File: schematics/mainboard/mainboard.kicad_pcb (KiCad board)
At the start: 4 copper layers, 88.5 x 180 mm, 94 parts, among them J1 SD_Card_Receptacle, J2 LCD_CONN, J3 USB_C_Receptacle_USB2.0_16P, J4 BATTERY_CONN, J6 HID_CONN, J7 SPEAKER, J8 TRACKBALL_CONN, J9 AudioJack3, P1 1-1473005-4, SW1 SW_SPST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

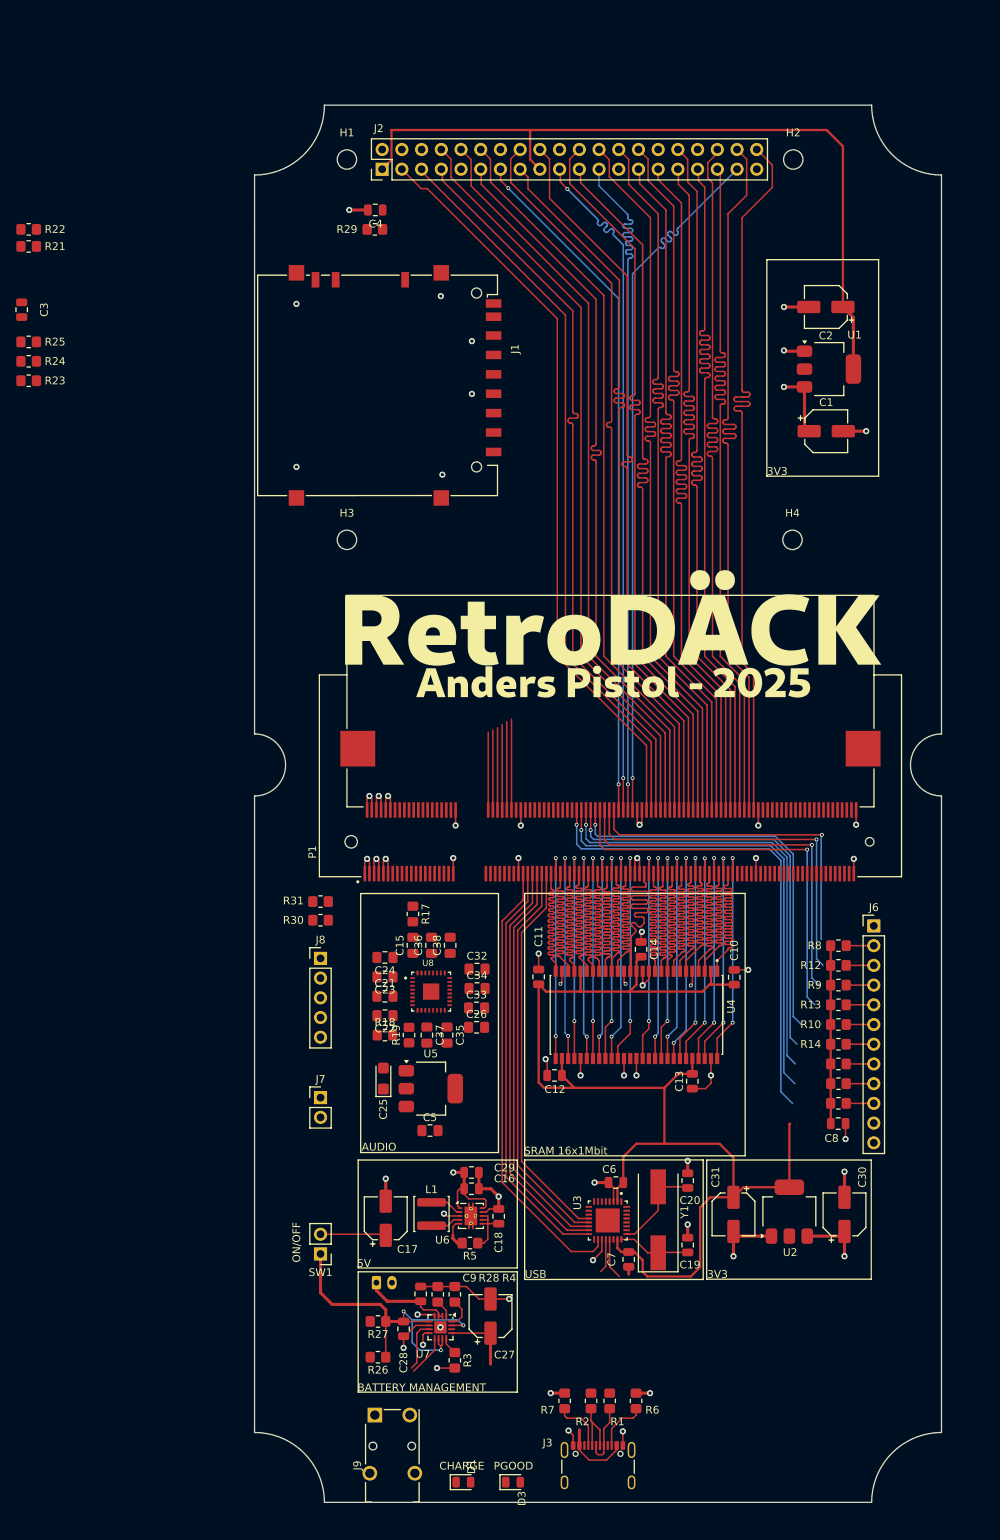
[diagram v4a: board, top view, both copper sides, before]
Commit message: Added "button board". Also placed LCD on main board at correct location.
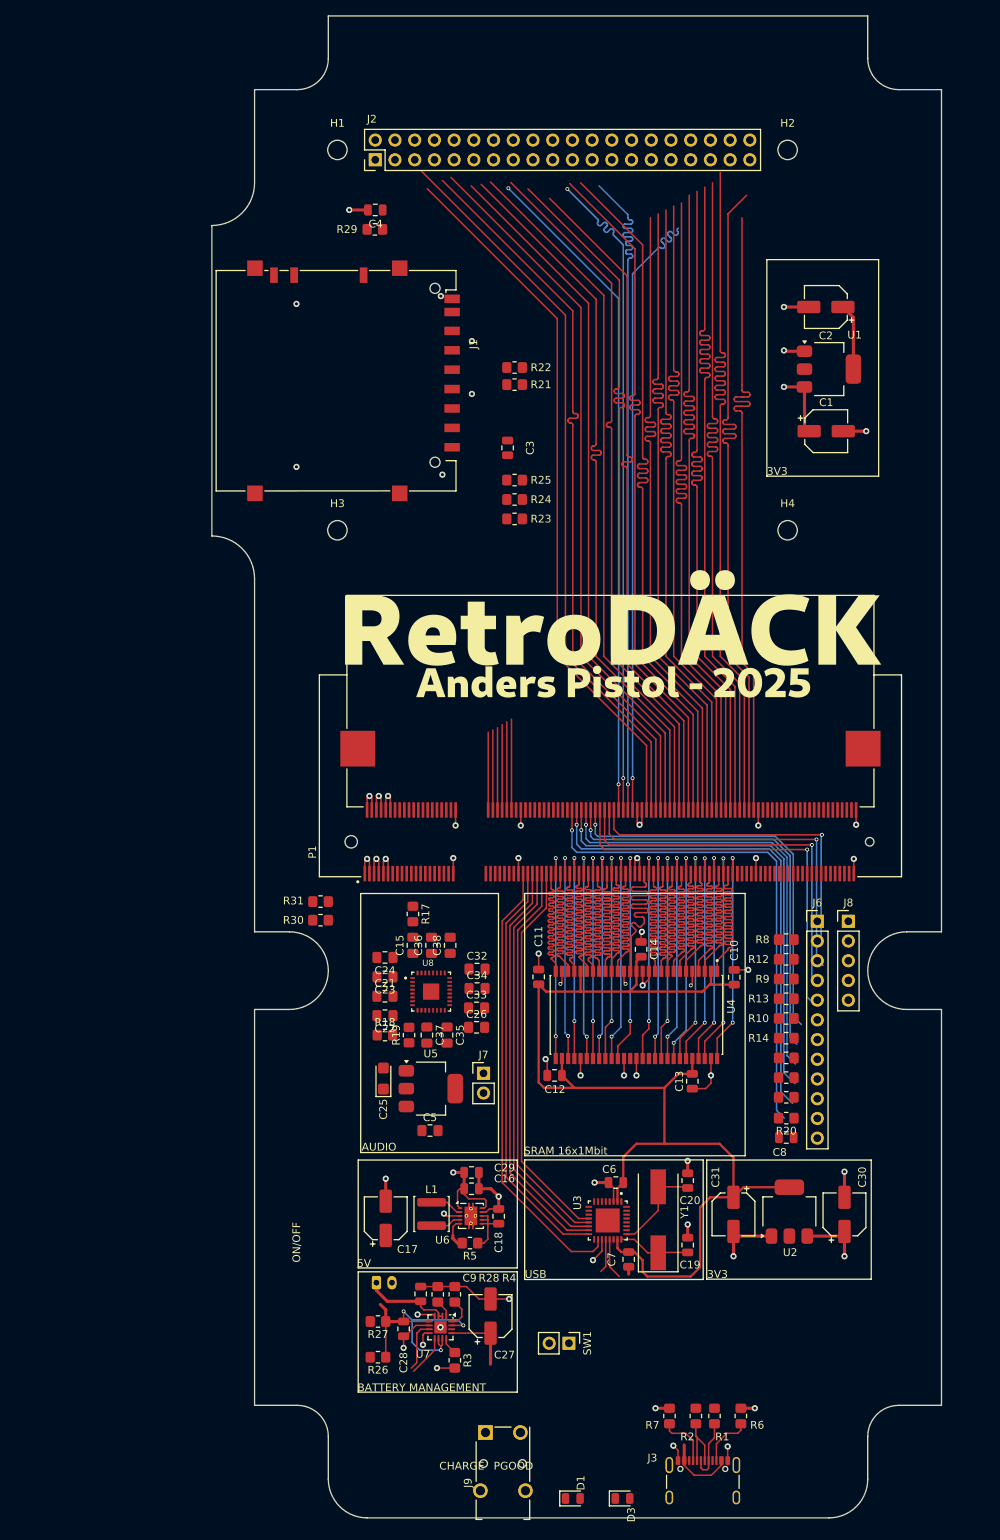
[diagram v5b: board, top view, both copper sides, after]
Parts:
- added R20: 10k, Resistor_SMD:R_0805_2012Metric_Pad1.20x1.40mm_HandSolder, F.Cu at (179.5, 230.5)
- moved J8 68.2 mm to (187.5, 205.1)
- moved C3 65.1 mm to (143.6, 144.2)
- moved R21 65.1 mm to (144.5, 136.0)
- moved R22 65.1 mm to (144.5, 133.8)
- moved R23 65.1 mm to (144.5, 153.3)
- moved R24 65.1 mm to (144.5, 150.8)
- moved R25 65.1 mm to (144.5, 148.3)
- moved SW1 34.0 mm to (151.5, 259.5), turned to -90 degrees
- moved J7 21.2 mm to (140.5, 224.7)
- moved J9 14.4 mm to (143.0, 277.5)
- moved D1 14.3 mm to (152.0, 279.5)
- moved D3 14.3 mm to (158.4, 279.5)
- moved J3 13.6 mm to (168.8, 278.3)
- moved R1 13.6 mm to (170.3, 268.9)
- moved R2 13.6 mm to (167.9, 268.9)
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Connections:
- J6 pad 11: unconnected-(J6-Pin_11-Pad11) -> HIO_BTN_RESET
- P1 pad 78: unconnected-(P1-Pad78) -> HIO_BTN_RESET
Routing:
- net 3V3_AUDIO: track 99.6 -> 8.64 mm
- net HIO_BTN_RESET: track 0.00 -> 65.4 mm, vias 0 -> 1
- net 3V3: track 175.5 -> 144.3 mm
- net Net-(SW1-A): track 47.0 -> 33.7 mm
- net LCD_B4: track 95.8 -> 84.2 mm
- net LCD_R1: track 95.0 -> 83.8 mm
- net LCD_PROG_DATA: track 91.8 -> 81.1 mm
- net LCD_B3: track 96.0 -> 85.6 mm
- net LCD_ENABLE: track 95.5 -> 86.3 mm
- net SYS_LOAD: track 12.5 -> 4.24 mm
- net LCD_R4: track 94.9 -> 88.1 mm
- net LCD_CLK: track 95.9 -> 89.2 mm
- net LCD_G0: track 95.2 -> 88.8 mm
- net LCD_R0: track 94.3 -> 87.9 mm
- net LCD_B1: track 95.4 -> 89.8 mm
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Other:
- board size 88.5 x 180 mm -> 94 x 193.5 mm

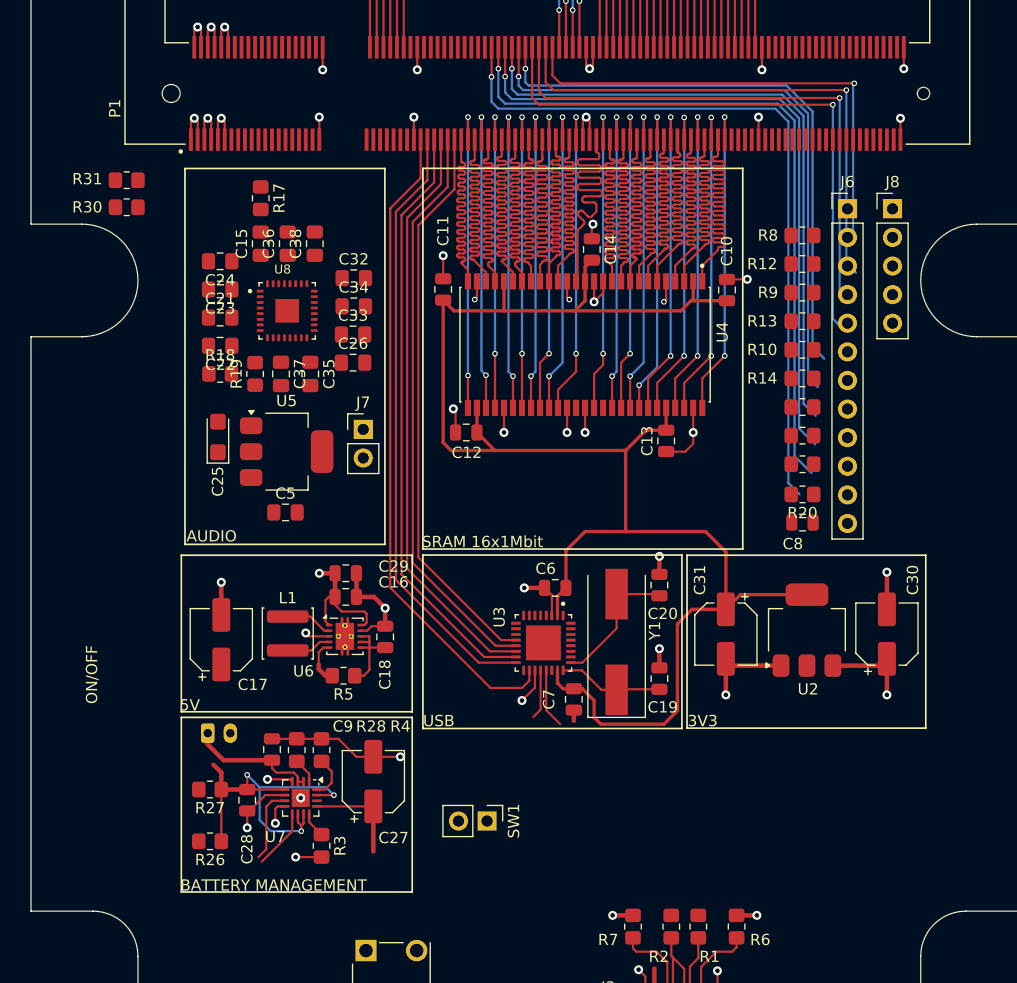
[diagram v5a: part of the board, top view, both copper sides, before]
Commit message: Flat flex connector for interconnect.
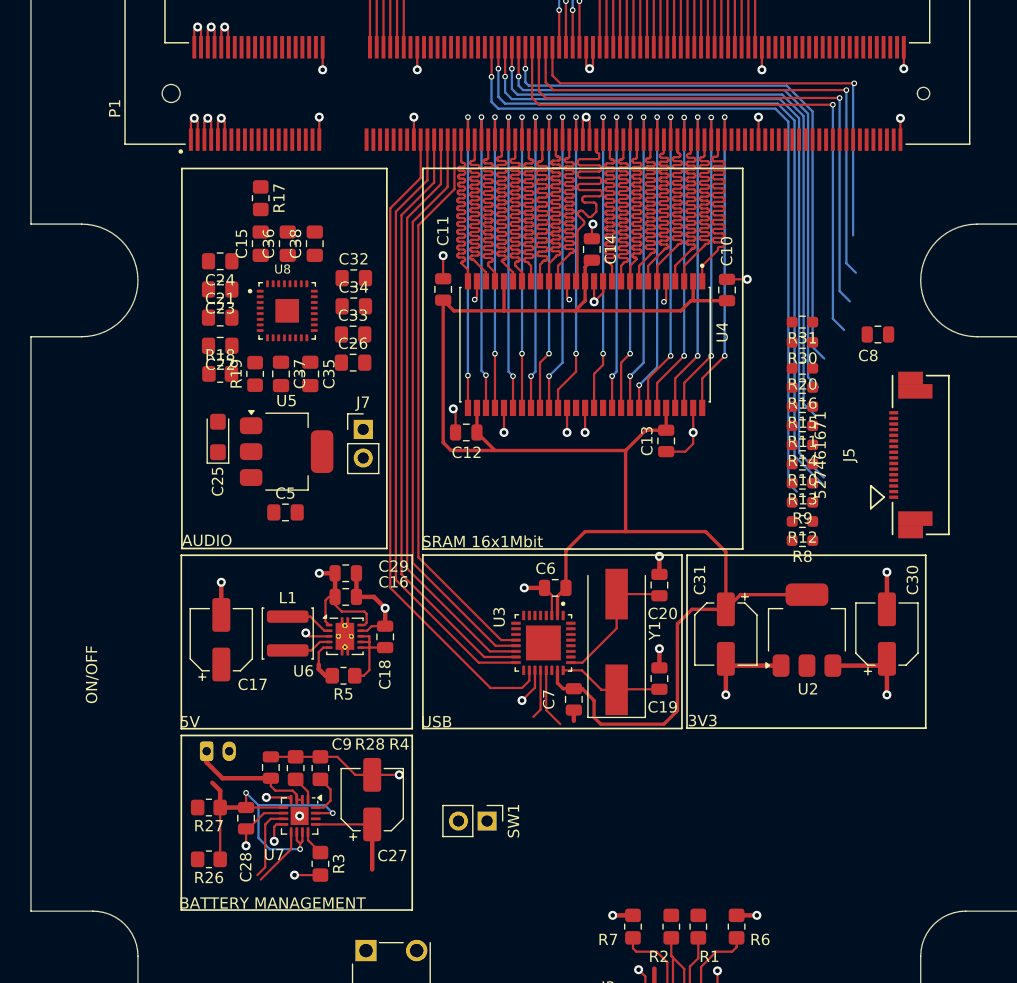
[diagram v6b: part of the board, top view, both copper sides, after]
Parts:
- removed J6: HID_CONN, Connector_PinHeader_2.54mm:PinHeader_1x12_P2.54mm_Vertical
- removed J8: TRACKBALL_CONN, Connector_PinHeader_2.54mm:PinHeader_1x05_P2.54mm_Vertical
- added J5: 527461671, CON_527461671_MOL:CON_527461671_MOL, F.Cu at (190.0, 227.0)
- R10, R11, R12, R13, R14, R15, R16, R20, R30, R31, R8, R9: footprint Resistor_SMD:R_0805_2012Metric_Pad1.20x1.40mm_HandSolder -> Resistor_SMD:R_0603_1608Metric_Pad0.98x0.95mm_HandSolder
- moved R31 61.3 mm to (179.5, 215.2)
- moved R30 61.2 mm to (179.5, 217.0)
- moved R8 27.1 mm to (179.5, 234.6)
- moved R12 22.9 mm to (179.5, 232.9)
- moved R9 18.6 mm to (179.5, 231.2)
- moved C8 18.0 mm to (186.2, 216.3)
- moved R13 14.4 mm to (179.5, 229.5)
- moved R20 11.2 mm to (179.5, 219.3)
- moved R10 10.1 mm to (179.5, 227.8)
- moved R16 6.82 mm to (179.5, 221.0)
- moved R14 5.90 mm to (179.5, 226.1)
- moved R15 2.58 mm to (179.5, 222.7)
- moved R11 1.66 mm to (179.5, 224.4)
- moved R3 1.60 mm to (136.7, 263.3)
- moved R4 1.60 mm to (136.7, 254.8)
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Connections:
- P1 pad 78: HIO_BTN_RESET -> HIO_DPAD_N
- P1 pad 80: HIO_BTN_X -> HIO_DPAD_S
- P1 pad 82: HIO_BTN_D -> HIO_DPAD_W
- P1 pad 84: HIO_BTN_C -> HIO_DPAD_E
- P1 pad 86: HIO_BTN_B -> HIO_BTN_A
- P1 pad 88: HIO_BTN_A -> HIO_BTN_B
- P1 pad 90: HIO_DPAD_E -> HIO_BTN_C
- P1 pad 92: HIO_DPAD_W -> HIO_BTN_D
- P1 pad 94: HIO_DPAD_S -> HIO_BTN_X
- P1 pad 96: HIO_DPAD_N -> HIO_BTN_RESET
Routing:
- net HIO_BTN_RESET: track 65.4 -> 43.1 mm
- net HIO_DPAD_N: track 43.1 -> 65.1 mm
- net HIO_DPAD_S: track 46.7 -> 64.9 mm
- net HIO_BTN_X: track 63.5 -> 46.7 mm
- net HIO_DPAD_W: track 49.3 -> 63.9 mm
- net HIO_BTN_D: track 60.6 -> 49.3 mm
- net HIO_DPAD_E: track 51.9 -> 57.7 mm
- net HIO_BTN_C: track 57.7 -> 51.9 mm
- net HIO_BTN_B: track 54.8 -> 52.0 mm
- net HIO_BTN_A: track 52.0 -> 54.8 mm

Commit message: Some cleanup in mainboard.
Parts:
- R1, R17, R18, R19, R2, R21, R22, R23, R24, R25, R26, R27, R28, R29, R3, R4, R6, R7: footprint Resistor_SMD:R_0805_2012Metric_Pad1.20x1.40mm_HandSolder -> Resistor_SMD:R_0603_1608Metric_Pad0.98x0.95mm_HandSolder
- moved SW1 136.2 mm to (202.0, 133.0), turned to 0 degrees
- moved C3 10.5 mm to (141.0, 134.0), turned to 180 degrees
- moved R25 9.94 mm to (141.0, 139.0)
- moved R24 9.84 mm to (141.0, 141.6)
- moved R21 9.84 mm to (141.0, 126.8)
- moved R23 9.75 mm to (141.0, 144.2)
- moved R22 9.66 mm to (141.0, 124.8)
- moved R10 6.07 mm to (178.6, 221.8)
- moved R11 6.07 mm to (178.6, 218.4)
- moved R12 6.07 mm to (178.6, 226.9)
- moved R13 6.07 mm to (178.6, 223.5)
- moved R14 6.07 mm to (178.6, 220.1)
- moved R15 6.07 mm to (178.6, 216.7)
- moved R16 6.07 mm to (178.6, 215.0)
- moved R20 6.07 mm to (178.6, 213.3)
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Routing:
- net Net-(U3-D-): track 4.41 -> 26.6 mm
- net Net-(U3-D+): track 5.30 -> 27.3 mm
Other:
- board size 94 x 193.5 mm -> 99.5 x 193.5 mm
